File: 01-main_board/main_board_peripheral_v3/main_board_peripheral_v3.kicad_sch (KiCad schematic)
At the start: 20 parts, among them J2 T4040014041000, J3 T4041017041-000, J4 FH41-15S-0.5SH_05_, Q1 SSF2302, U1 LM74610QDGKRQ1

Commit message: Completed draft of main peripheral v3
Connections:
- net GND: now also J4.G3
- net RX_N: now also J4.11; no longer J4.10
- net RX_P: now also J4.10; no longer J4.11
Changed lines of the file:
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@@
 	(global_label "RX_P"
 		(shape bidirectional)
-		(at 80.01 161.29 0)
+		(at 80.01 158.75 0)
 		(fields_autoplaced yes)
 		(effects
@@
 		)
 		(property "Intersheetrefs" "${INTERSHEET_REFS}"
-			(at 88.8236 161.29 0)
+			(at 88.8236 158.75 0)
 			(effects
 				(font
@@
 	(global_label "RX_N"
 		(shape bidirectional)
-		(at 80.01 158.75 0)
+		(at 80.01 161.29 0)
 		(fields_autoplaced yes)
 		(effects
@@
 		)
 		(property "Intersheetrefs" "${INTERSHEET_REFS}"
-			(at 88.8841 158.75 0)
+			(at 88.8841 161.29 0)
 			(effects
 				(font
@@
 					(unit 1)
 				)
+			)
+		)
+	)
+	(symbol
+		(lib_id "power:GND")
+		(at 54.61 156.21 270)
+		(unit 1)
+		(exclude_from_sim no)
+		(in_bom yes)
+		(on_board yes)
+		(dnp no)
+		(fields_autoplaced yes)
+		(property "Reference" "#PWR010"
+			(at 48.26 156.21 0)
+			(effects
+				(font
+					(size 1.27 1.27)
+				)
+				(hide yes)
+			)
+		)
+		(property "Value" "GND"
+			(at 49.53 156.21 0)
+			(effects
+				(font
+					(size 1.27 1.27)
+				)
+				(hide yes)
+			)
+		)
+		(property "Footprint" ""
+			(at 54.61 156.21 0)
+			(effects
+				(font
+					(size 1.27 1.27)
+				)
+				(hide yes)
+			)
+		)
+		(property "Datasheet" ""
+			(at 54.61 156.21 0)
+			(effects
+				(font
+					(size 1.27 1.27)
+				)
+				(hide yes)
+			)
+		)
+		(property "Description" "Power symbol creates a global label with name \"GND\" , ground"
+			(at 54.61 156.21 0)
+			(effects
+				(font
+					(size 1.27 1.27)
+				)
+				(hide yes)
+			)
+		)
+		(pin "1"
+		)
+		(instances
+			(project "main_board_peripheral_v3"
+				(path "/3f673207-cdae-494a-ab60-6e58b06fb202"
+					(reference "#PWR010")
+					(unit 1)
+				)

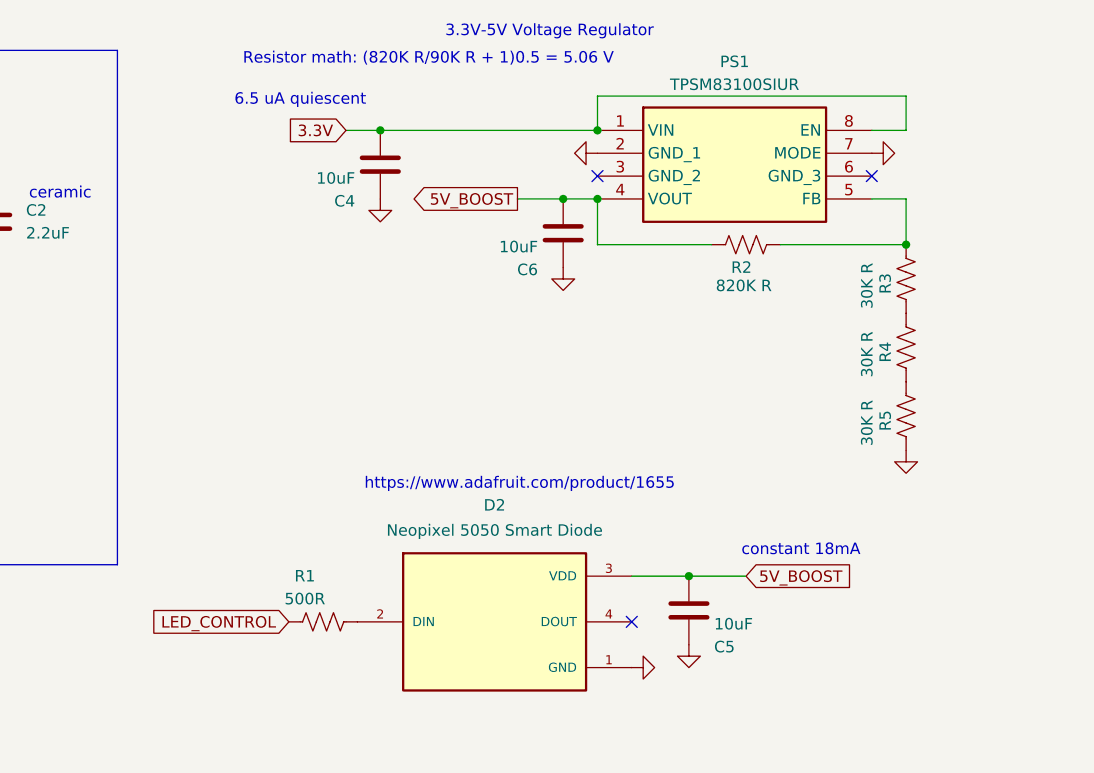
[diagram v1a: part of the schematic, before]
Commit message: Completed main peripheral edits
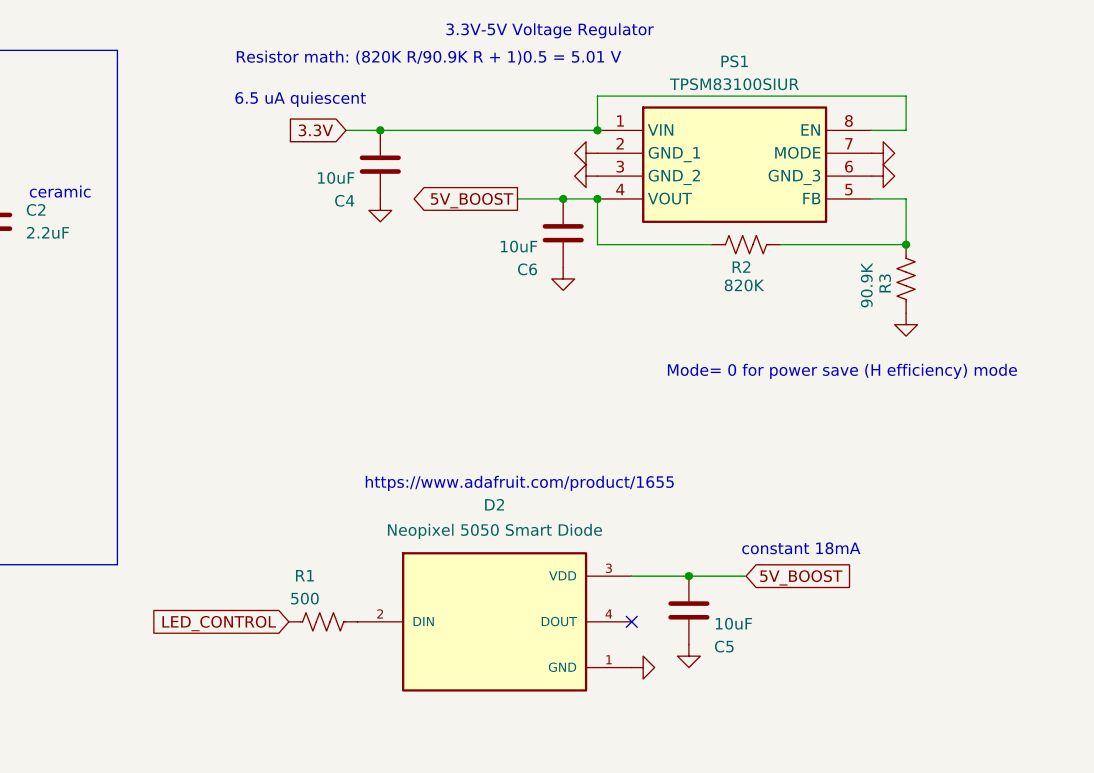
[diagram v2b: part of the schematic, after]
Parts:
- removed R4, R5: 30K R, 22XT_Main_Peripheral:RESC3116X65N (30K), symbol Device:R_US
- R1: value 500R -> 500
- R2: value 820K R -> 820K; footprint 22XT_Main_Peripheral:RESC3116X65N (820K) -> Resistor_SMD:R_0603_1608Metric
- R3: value 30K R -> 90.9K; footprint 22XT_Main_Peripheral:RESC3116X65N (30K) -> Resistor_SMD:R_0603_1608Metric
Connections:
- net GND: now also PS1.3 (GND_2), PS1.6 (GND_3), R3.1
- no-connect marks 5 -> 3
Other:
- note added: "Mode= 0 for power save (H efficiency) mode"
- note added: "Resistor math: (820K R/90.9K R + 1)0.5 = 5.01 V"
- note removed: "Resistor math: (820K R/90K R + 1)0.5 = 5.06 V"
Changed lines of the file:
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@@
 		)
 	)
-	(text "Resistor math: (820K R/90K R + 1)0.5 = 5.06 V"
+	(text "Resistor math: (820K R/90.9K R + 1)0.5 = 5.01 V"
 		(exclude_from_sim no)
 		(at 214.884 20.066 0)
@@
 		)
 	)
+	(text "Mode= 0 for power save (H efficiency) mode"
+		(exclude_from_sim no)
+		(at 260.858 54.864 0)
+		(effects
+			(font
+				(size 1.27 1.27)
+			)
+		)
+	)
 	(text "6.5 uA quiescent"
 		(exclude_from_sim no)
@@
 	)
 	(no_connect
-		(at 264.16 33.02)
-	)
-	(no_connect
-		(at 233.68 33.02)
-	)
-	(no_connect
 		(at 29.21 36.83)
 	)
@@
 	(symbol
 		(lib_id "power:GND")
-		(at 267.97 63.5 0)
+		(at 267.97 48.26 0)
 		(unit 1)
 		(exclude_from_sim no)
@@
 		(fields_autoplaced yes)
 		(property "Reference" "#PWR012"
-			(at 267.97 69.85 0)
+			(at 267.97 54.61 0)
 			(effects
 				(font
@@
 		)
 		(property "Value" "GND"
-			(at 267.97 68.58 0)
+			(at 267.97 53.34 0)
 			(effects
 				(font
@@
 		)
 		(property "Footprint" ""
-			(at 267.97 63.5 0)
+			(at 267.97 48.26 0)
 			(effects
 				(font
@@
 		)
 		(property "Datasheet" ""
-			(at 267.97 63.5 0)
+			(at 267.97 48.26 0)
 			(effects
 				(font
@@
 		)
 		(property "Description" "Power symbol creates a global label with name \"GND\" , ground"
-			(at 267.97 63.5 0)
+			(at 267.97 48.26 0)
 			(effects
 				(font
@@
 			)
 		)
-		(property "Value" "820K R"
+		(property "Value" "820K"
 			(at 249.936 45.212 90)
 			(effects
@@
 			)
 		)
-		(property "Footprint" "22XT_Main_Peripheral:RESC3116X65N (820K)"
+		(property "Footprint" "Resistor_SMD:R_0603_1608Metric"
 			(at 249.936 41.656 90)
 			(effects
@@
 	(symbol
 		(lib_id "power:GND")
+		(at 233.68 33.02 270)
+		(unit 1)
+		(exclude_from_sim no)
+		(in_bom yes)
+		(on_board yes)
+		(dnp no)
+		(fields_autoplaced yes)
+		(property "Reference" "#PWR013"
+			(at 227.33 33.02 0)
+			(effects
+				(font
+					(size 1.27 1.27)
+				)
+				(hide yes)
+			)
+		)
+		(property "Value" "GND"
+			(at 229.87 33.0199 90)
+			(effects
+				(font
+					(size 1.27 1.27)
+				)
+				(justify right)
+				(hide yes)
+			)
+		)
+		(property "Footprint" ""
+			(at 233.68 33.02 0)
+			(effects
+				(font
+					(size 1.27 1.27)
+				)
+				(hide yes)
+			)
+		)
+		(property "Datasheet" ""
+			(at 233.68 33.02 0)
+			(effects
+				(font
+					(size 1.27 1.27)
+				)
+				(hide yes)
+			)
+		)
+		(property "Description" "Power symbol creates a global label with name \"GND\" , ground"
+			(at 233.68 33.02 0)
+			(effects
+				(font
+					(size 1.27 1.27)
+				)
+				(hide yes)
+			)
+		)
+		(pin "1"
+		)
+		(instances
+			(project "main_board_peripheral_v3"
+				(path "/3f673207-cdae-494a-ab60-6e58b06fb202"
+					(reference "#PWR013")
+					(unit 1)
+				)
+			)
+		)
+	)
+	(symbol
+		(lib_id "power:GND")
 		(at 39.37 52.07 90)
 		(unit 1)
@@
 	)
 	(symbol
+		(lib_id "power:GND")
+		(at 264.16 33.02 90)
+		(unit 1)
+		(exclude_from_sim no)
+		(in_bom yes)
+		(on_board yes)
+		(dnp no)
+		(fields_autoplaced yes)
+		(property "Reference" "#PWR014"
+			(at 270.51 33.02 0)
+			(effects
+				(font
+					(size 1.27 1.27)
+				)
+				(hide yes)
+			)
+		)
+		(property "Value" "GND"
+			(at 267.97 33.0201 90)
+			(effects
+				(font
+					(size 1.27 1.27)
+				)
+				(justify right)
+				(hide yes)
+			)
+		)
+		(property "Footprint" ""
+			(at 264.16 33.02 0)
+			(effects
+				(font
+					(size 1.27 1.27)
+				)
+				(hide yes)
+			)
+		)
+		(property "Datasheet" ""
+			(at 264.16 33.02 0)
+			(effects
+				(font
+					(size 1.27 1.27)
+				)
+				(hide yes)
+			)
+		)
+		(property "Description" "Power symbol creates a global label with name \"GND\" , ground"
+			(at 264.16 33.02 0)
+			(effects
+				(font
+					(size 1.27 1.27)
+				)
+				(hide yes)
+			)
+		)
+		(pin "1"
+		)
+		(instances
+			(project "main_board_peripheral_v3"
+				(path "/3f673207-cdae-494a-ab60-6e58b06fb202"
+					(reference "#PWR014")
+					(unit 1)
+				)
+			)
+		)
+	)
+	(symbol
 		(lib_id "Transistor_FET:2N7002K")
 		(at 87.63 58.42 270)
@@
 	)
 	(symbol
-		(lib_id "Device:R_US")
-		(at 267.97 59.69 180)
-		(unit 1)
-		(exclude_from_sim no)
-		(in_bom yes)
-		(on_board yes)
-		(dnp no)
-		(property "Reference" "R5"
-			(at 265.684 60.198 90)
-			(effects
-				(font
-					(size 1.27 1.27)
-				)
-			)
-		)
-		(property "Value" "30K R"
-			(at 263.652 60.452 90)
-			(effects
-				(font
-					(size 1.27 1.27)
-				)
-			)
-		)
-		(property "Footprint" "22XT_Main_Peripheral:RESC3116X65N (30K)"
-			(at 266.954 59.436 90)
-			(effects
-				(font
-					(size 1.27 1.27)
-				)
-				(hide yes)
-			)
-		)
-		(property "Datasheet" "~"
-			(at 267.97 59.69 0)
-			(effects
-				(font
-					(size 1.27 1.27)
-				)
-				(hide yes)
-			)
-		)
-		(property "Description" "Resistor, US symbol"
-			(at 267.97 59.69 0)
-			(effects
-				(font
-					(size 1.27 1.27)
-				)
-				(hide yes)
-			)
-		)
-		(pin "1"
-		)
-		(pin "2"
-		)
-		(instances
-			(project "main_board_peripheral_v2"
-				(path "/3f673207-cdae-494a-ab60-6e58b06fb202"
-					(reference "R5")
-					(unit 1)
-				)
-			)
-		)
-	)
-	(symbol
 		(lib_id "power:GND")
 		(at 80.01 143.51 90)
@@
 			)
 		)
-		(property "Value" "500R"
+		(property "Value" "500"
 			(at 201.168 80.01 90)
 			(effects
@@
 	)
 	(symbol
-		(lib_id "Device:R_US")
-		(at 267.97 52.07 180)
-		(unit 1)
-		(exclude_from_sim no)
-		(in_bom yes)
-		(on_board yes)
-		(dnp no)
-		(property "Reference" "R4"
-			(at 265.684 52.578 90)
-			(effects
-				(font
-					(size 1.27 1.27)
-				)
-			)
-		)
-		(property "Value" "30K R"
-			(at 263.652 52.832 90)
-			(effects
-				(font
-					(size 1.27 1.27)
-				)
-			)
-		)
-		(property "Footprint" "22XT_Main_Peripheral:RESC3116X65N (30K)"
-			(at 266.954 51.816 90)
-			(effects
-				(font
-					(size 1.27 1.27)
-				)
-				(hide yes)
-			)
-		)
-		(property "Datasheet" "~"
-			(at 267.97 52.07 0)
-			(effects
-				(font
-					(size 1.27 1.27)
-				)
-				(hide yes)
-			)
-		)
-		(property "Description" "Resistor, US symbol"
-			(at 267.97 52.07 0)
-			(effects
-				(font
-					(size 1.27 1.27)
-				)
-				(hide yes)
-			)
-		)
-		(pin "1"
-		)
-		(pin "2"
-		)
-		(instances
-			(project "main_board_peripheral_v2"
-				(path "/3f673207-cdae-494a-ab60-6e58b06fb202"
-					(reference "R4")
-					(unit 1)
-				)
-			)
-		)
-	)
-	(symbol
 		(lib_id "power:GND")
 		(at 233.68 30.48 270)
@@
 			)
 		)
-		(property "Value" "30K R"
+		(property "Value" "90.9K"
 			(at 263.652 45.212 90)
 			(effects
@@
 			)
 		)
-		(property "Footprint" "22XT_Main_Peripheral:RESC3116X65N (30K)"
+		(property "Footprint" "Resistor_SMD:R_0603_1608Metric"
 			(at 266.954 44.196 90)
 			(effects
